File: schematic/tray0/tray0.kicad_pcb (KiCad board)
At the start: 2 copper layers, 36.8 x 100.3 mm, 16 parts, among them J2 Conn_02x10_Odd_Even, J3 USB_B, P1 Mini-DIN_6pins_ver2, SW1 SW_SPST, U1 ATmega32U4-AU, U2 ST485EBDR, Y1 16MHz

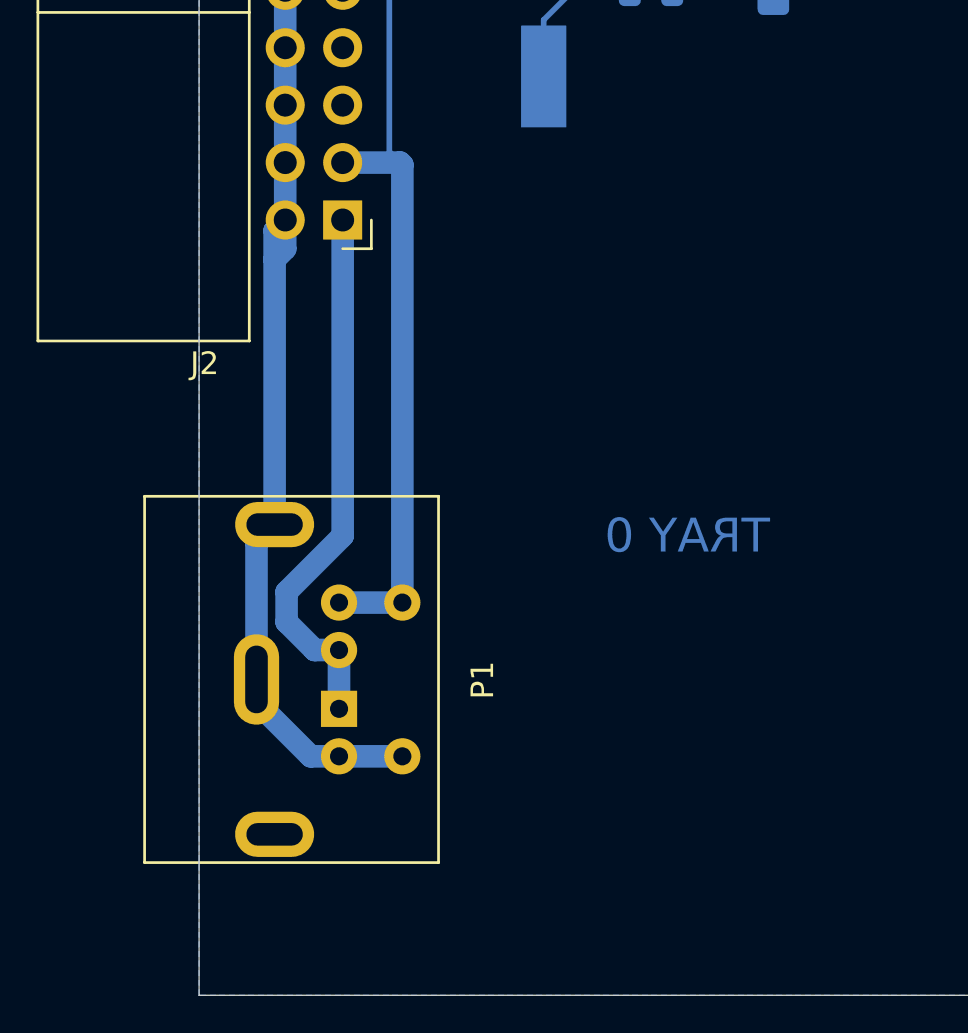
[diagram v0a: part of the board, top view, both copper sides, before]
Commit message: Add capacitors to board and change power connector to used by beefier PSU
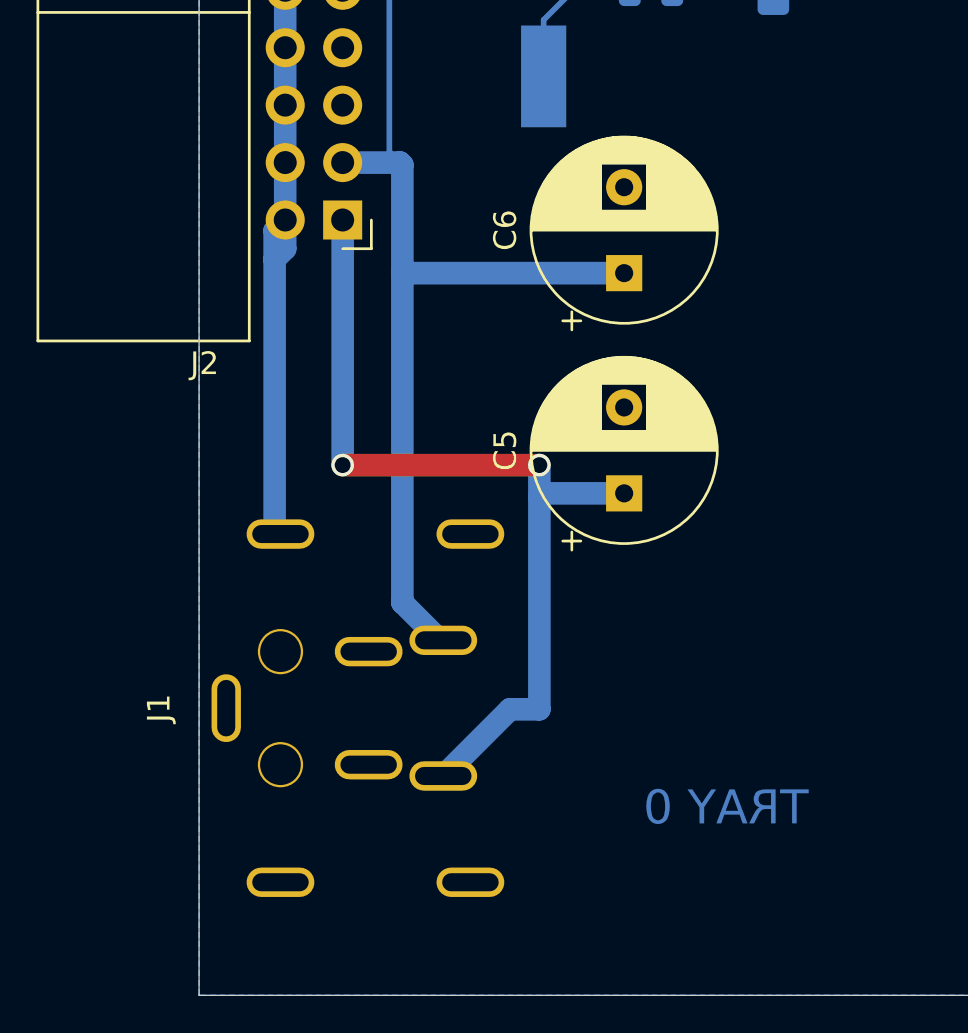
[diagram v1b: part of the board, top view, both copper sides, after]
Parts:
- removed P1: Mini-DIN_6pins_ver2, Custom_Footprints:Connector_Mini-DIN_Female_6Pin_2rows
- added C5: 470uF/25, Capacitor_THT:CP_Radial_D8.0mm_P3.80mm, F.Cu at (42.9, 167.0)
- added C6: 470uF/25V, Capacitor_THT:CP_Radial_D8.0mm_P3.80mm, F.Cu at (42.9, 157.3)
- added J1: Conn_01x05, tray0:PC-MDJ-402-4P, F.Cu at (24.1, 176.5)
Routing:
- net GND: track 70.6 -> 55.0 mm
- net +12V: track 24.2 -> 39.6 mm, vias 0 -> 2
- net +5V: track 42.9 -> 52.5 mm
